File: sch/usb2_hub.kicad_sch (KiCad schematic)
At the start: 49 parts, among them J10 USB_A, J6 USB_A, J7 USB_A, J8 USB_B, J9 USB_A, Q2 2N7002P, U5 MIC2026-1BM, U6 MIC2026-1BM, U7 USB2514B_Bi, Y2 24MHz

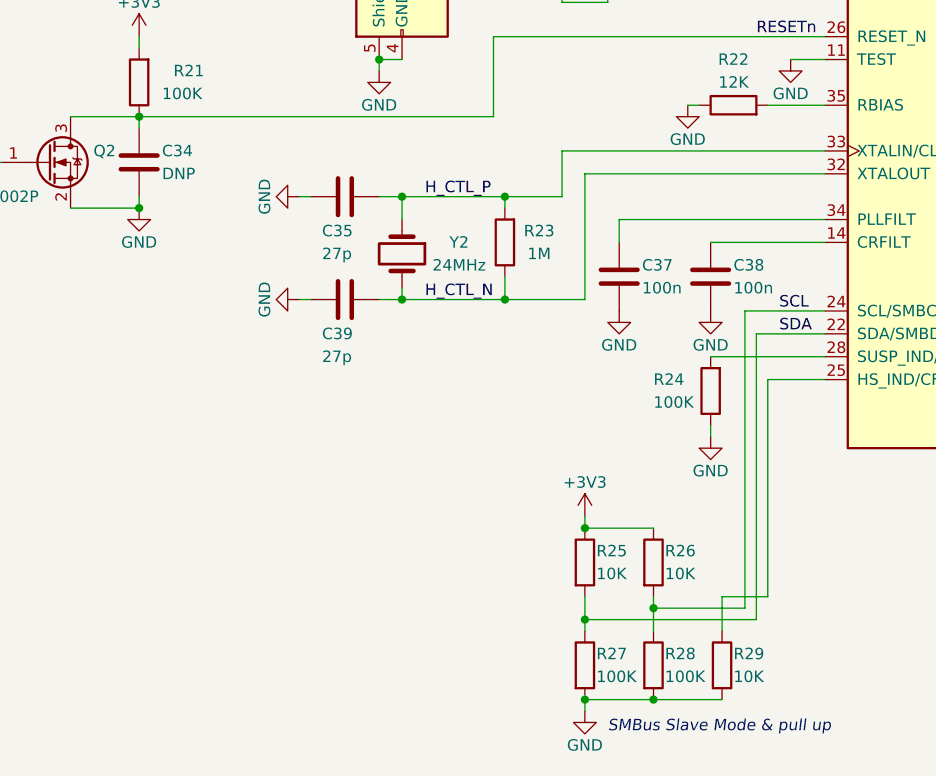
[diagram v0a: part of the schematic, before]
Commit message: added more DNF components for easy debugging
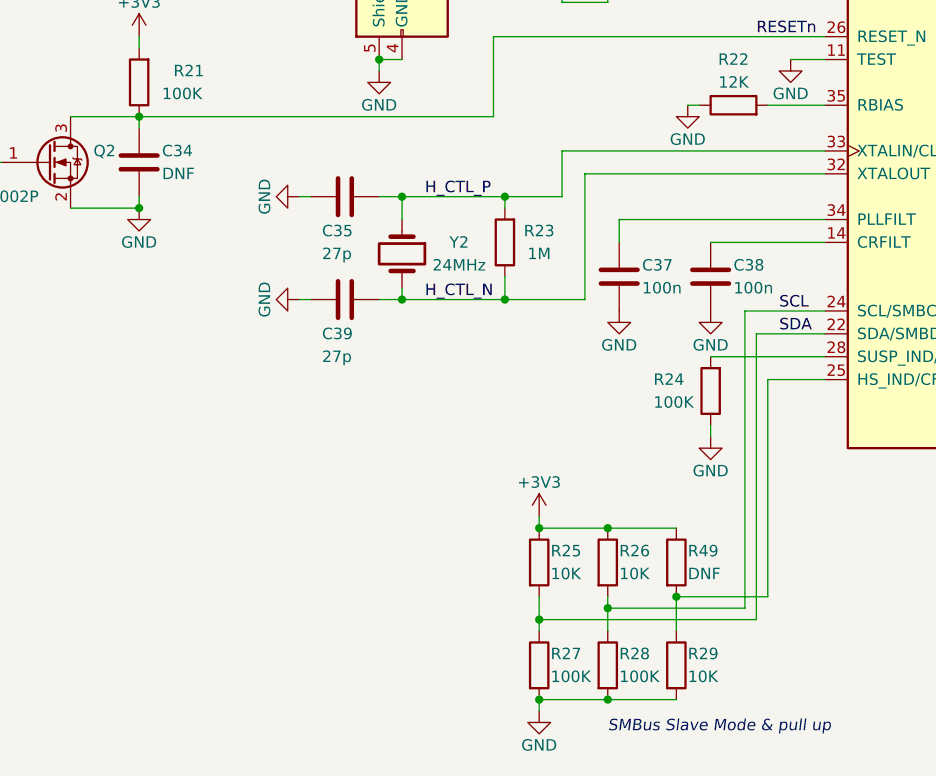
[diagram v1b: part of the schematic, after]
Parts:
- added R49: DNF, Resistor_SMD:R_0603_1608Metric_Pad0.98x0.95mm_HandSolder, symbol Device:R
- C34: value DNP -> DNF
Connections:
- net +3V3: now also R49.1
- net at R29.1, U7.25 (HS_IND/CFG_SEL1): now also R49.2
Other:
- moved on the sheet: R25, R26, R27, R28, R29
